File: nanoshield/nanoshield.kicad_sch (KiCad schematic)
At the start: 8 parts, among them J1 Conn_01x20_Socket, J2 Joy, J3 Conn_01x20_Socket, J4 M0S, J5 DIN-5_180degree

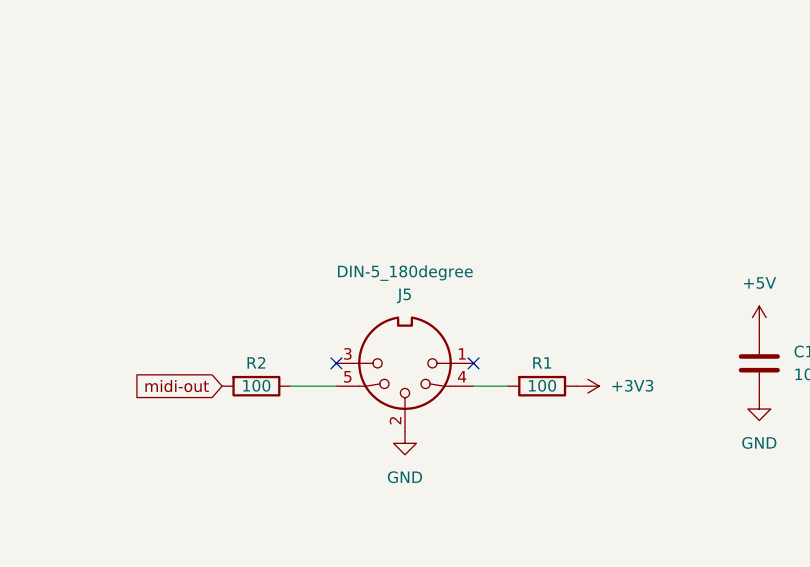
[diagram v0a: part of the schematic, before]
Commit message: relocation of some components
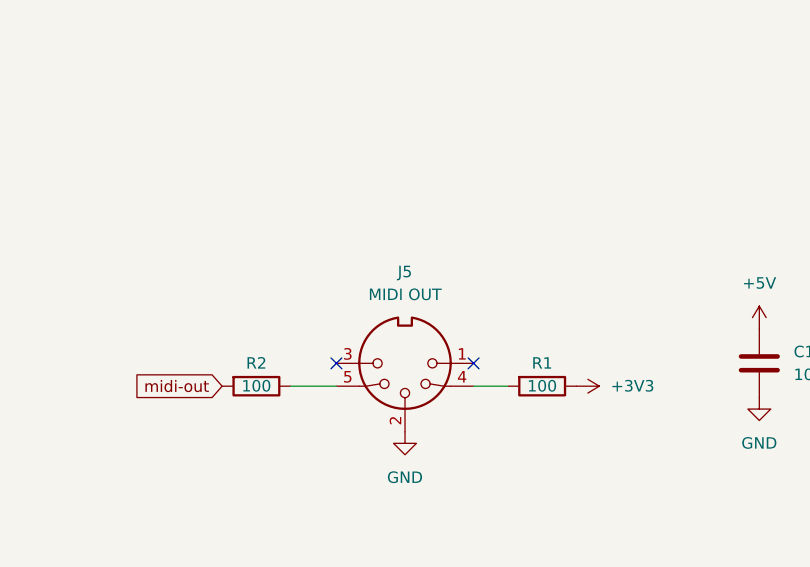
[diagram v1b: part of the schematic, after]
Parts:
- J5: value DIN-5_180degree -> MIDI OUT
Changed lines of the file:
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@@
   (symbol (lib_id "Connector:DIN-5_180degree") (at 187.96 83.82 180) (unit 1)
     (in_bom yes) (on_board yes) (dnp no) (fields_autoplaced)
-    (property "Reference" "J5" (at 187.9599 76.2 0)
+    (property "Reference" "J5" (at 187.9599 73.66 0)
       (effects (font (size 1.27 1.27)))
     )
-    (property "Value" "DIN-5_180degree" (at 187.9599 73.66 0)
+    (property "Value" "MIDI OUT" (at 187.9599 76.2 0)
       (effects (font (size 1.27 1.27)))
     )

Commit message: vcc on JOY temp removed
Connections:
- net +5V: no longer J2.7
- no-connect marks 31 -> 32
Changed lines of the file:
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@@
   (no_connect (at 81.28 66.04))
   (no_connect (at 121.92 40.64))
+  (no_connect (at 48.26 40.64))
   (no_connect (at 81.28 40.64))
   (no_connect (at 48.26 27.94))
@@
         )
       )
-    )
-  )
-  (symbol (lib_id "power:+5V") (at 48.26 40.64 270) (unit 1)
-    (in_bom yes) (on_board yes) (dnp no) (fields_autoplaced)
-    (property "Reference" "#PWR07" (at 44.45 40.64 0)
-      (effects (font (size 1.27 1.27)) hide)
-    )
-    (property "Value" "+5V" (at 52.07 40.64 90)
-      (effects (font (size 1.27 1.27)) (justify left))
-    )
-    (property "Footprint" "" (at 48.26 40.64 0)
-      (effects (font (size 1.27 1.27)) hide)
-    )
-    (property "Datasheet" "" (at 48.26 40.64 0)
-      (effects (font (size 1.27 1.27)) hide)
-    )
-    (pin "1")
-    (instances
-      (project "nanoshield"
-        (path "/279bcb58-e73f-4762-9835-ca58a1be9acb"
-          (reference "#PWR07") (unit 1)
-        )
-      )
